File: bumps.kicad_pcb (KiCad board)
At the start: 2 copper layers, 111.1 x 65.4 mm, 126 parts, among them M1 CONN_1, M2 CONN_1, M3 CONN_1, P1 Micro-E, P10 Mot-A, P11 Mot-A, P12 Mot-X, P13 T1, P14 T2, P15 T3, P16 MPower, P17 PWM-2, P18 PWM-1, P19 END-X, P2 DIL6, P20 END-Y, P21 END-Z, P22 Mot-X, P23 Mot-Y, P24 Mot-Y, P25 Mot-Z, P26 Mot-Z, P27 Aux, P29 PWM, P3 Mot-E, P4 Mot-E, P5 DIL6, P6 DIL6, P7 DIL6, P8 P8 Header, P9 P9 Header, Q1 N-FET, Q2 N-FET, Q3 FDS9926A, Q4 FDS9926A, U1 E-Polo, U2 A-Polo, U3 X-Polo, U4 Y-Polo, U5 Z-Polo, U6 MC34063, U7 AP1117/3.3

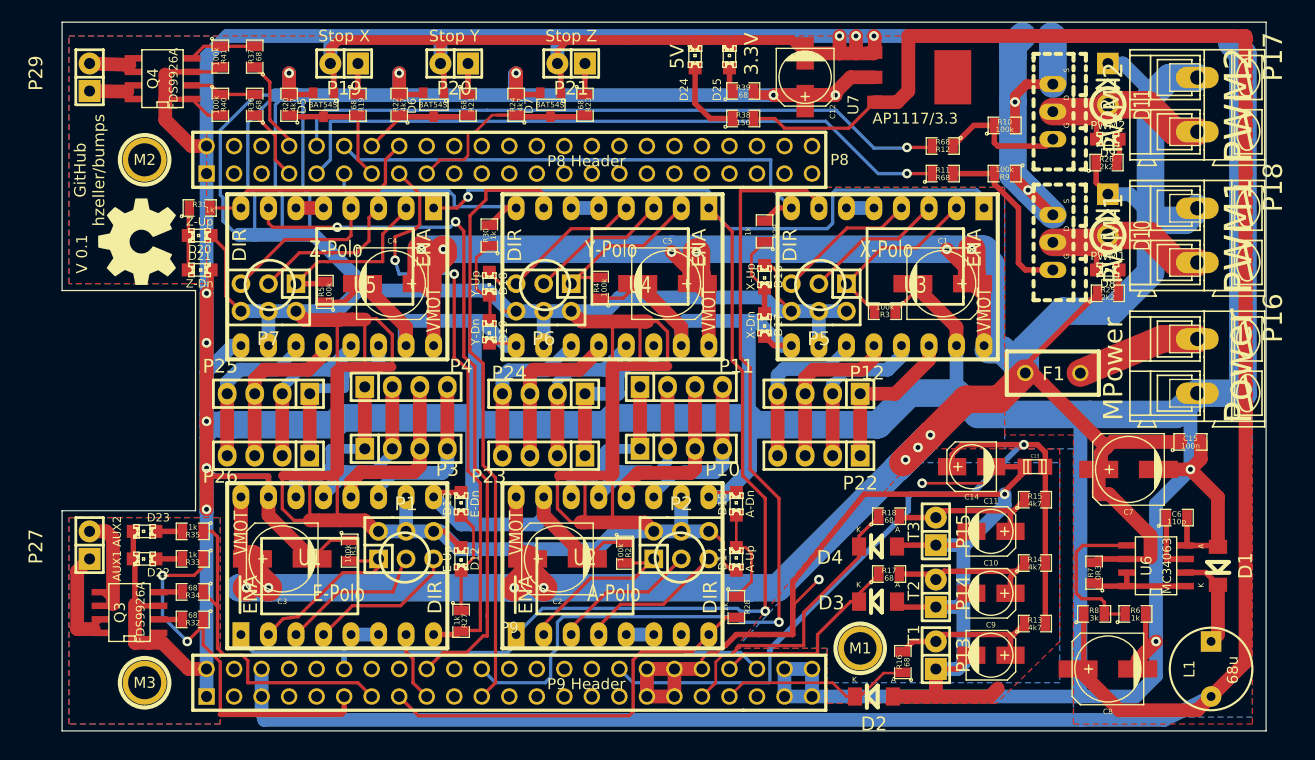
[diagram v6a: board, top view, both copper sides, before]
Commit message: o Route the new capacitors and resistors.
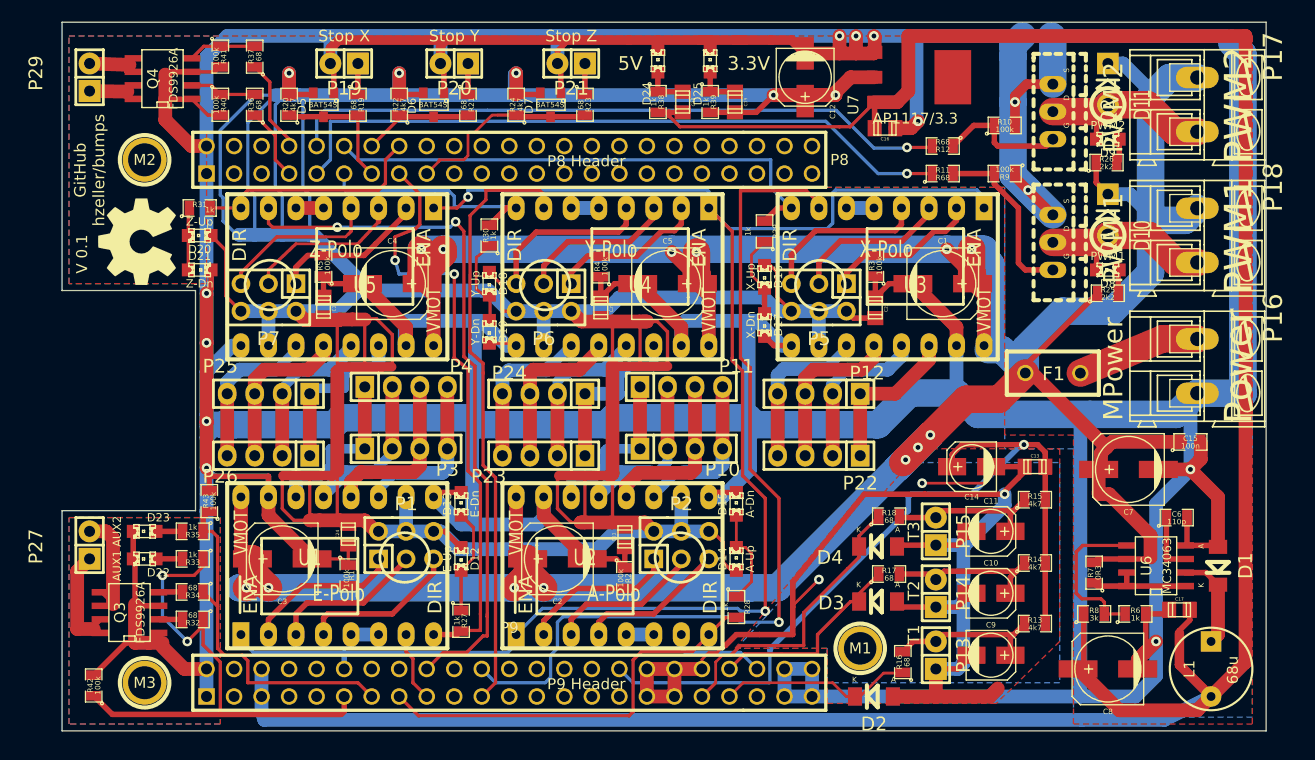
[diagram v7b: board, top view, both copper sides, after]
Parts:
- added C16: 100n, Capacitors_SMD:c_0805, F.Cu at (123.6, 37.7)
- added C17: 100n, Capacitors_SMD:c_0805, F.Cu at (150.7, 82.2)
- added C18: 100n, Capacitors_SMD:c_0805, F.Cu at (104.9, 35.3)
- added C19: 100n, Capacitors_SMD:c_0805, F.Cu at (109.7, 35.3)
- added C20: 100n, Capacitors_SMD:c_0805, F.Cu at (97.3, 54.3)
- added C21: 100n, Capacitors_SMD:c_0805, F.Cu at (99.6, 75.4)
- added C22: 100n, Capacitors_SMD:c_0805, F.Cu at (71.8, 54.2)
- added C23: 100n, Capacitors_SMD:c_0805, F.Cu at (122.7, 54.3)
- added C24: 100n, Capacitors_SMD:c_0805, F.Cu at (74.0, 75.2)
- added R42: 100k, SMD_Packages:SM0805, F.Cu at (50.5, 89.2)
- added R43: 100k, SMD_Packages:SM0805, F.Cu at (61.2, 72.1)
- R38: value 150 -> 1k
- R39: value 68 -> 1k
- moved R38 8.02 mm to (102.6, 35.3), turned to 270 degrees
- moved R3 4.28 mm to (122.7, 50.4), turned to 90 degrees
- moved D24 3.45 mm to (102.6, 31.5)
- moved R39 3.21 mm to (107.4, 35.3), turned to 270 degrees
- moved R5 2.42 mm to (71.8, 50.4)
- moved R2 2.35 mm to (99.6, 79.2)
- moved R1 2.29 mm to (74.0, 79.0)
- moved R4 1.97 mm to (97.3, 50.5)
- moved D25 1.82 mm to (107.4, 31.5)
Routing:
- net GND: track 809.0 -> 835.2 mm
- net VDD_5V: track 226.9 -> 249.3 mm
- net VDD_3V3: track 425.0 -> 444.1 mm
- net AUX_1: track 37.3 -> 49.7 mm
- net Net-(C18-Pad2): track 7.34 -> 4.09 mm
- net Net-(P7-Pad1): track 17.5 -> 14.6 mm
- net Net-(P6-Pad3): track 13.1 -> 15.7 mm
- net Net-(P5-Pad3): track 13.1 -> 15.5 mm
- net Net-(P5-Pad1): track 16.7 -> 14.3 mm
- net AUX_2: track 31.0 -> 33.1 mm
- net Net-(C19-Pad2): track 2.26 -> 4.09 mm
- net Net-(P1-Pad1): track 16.3 -> 14.6 mm
- net Net-(P5-Pad2): track 13.1 -> 14.5 mm
- net Net-(P6-Pad2): track 13.1 -> 14.5 mm
- net Net-(P6-Pad1): track 16.0 -> 14.5 mm
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
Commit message: o More copper around pads    - fuse    - mounting holes.
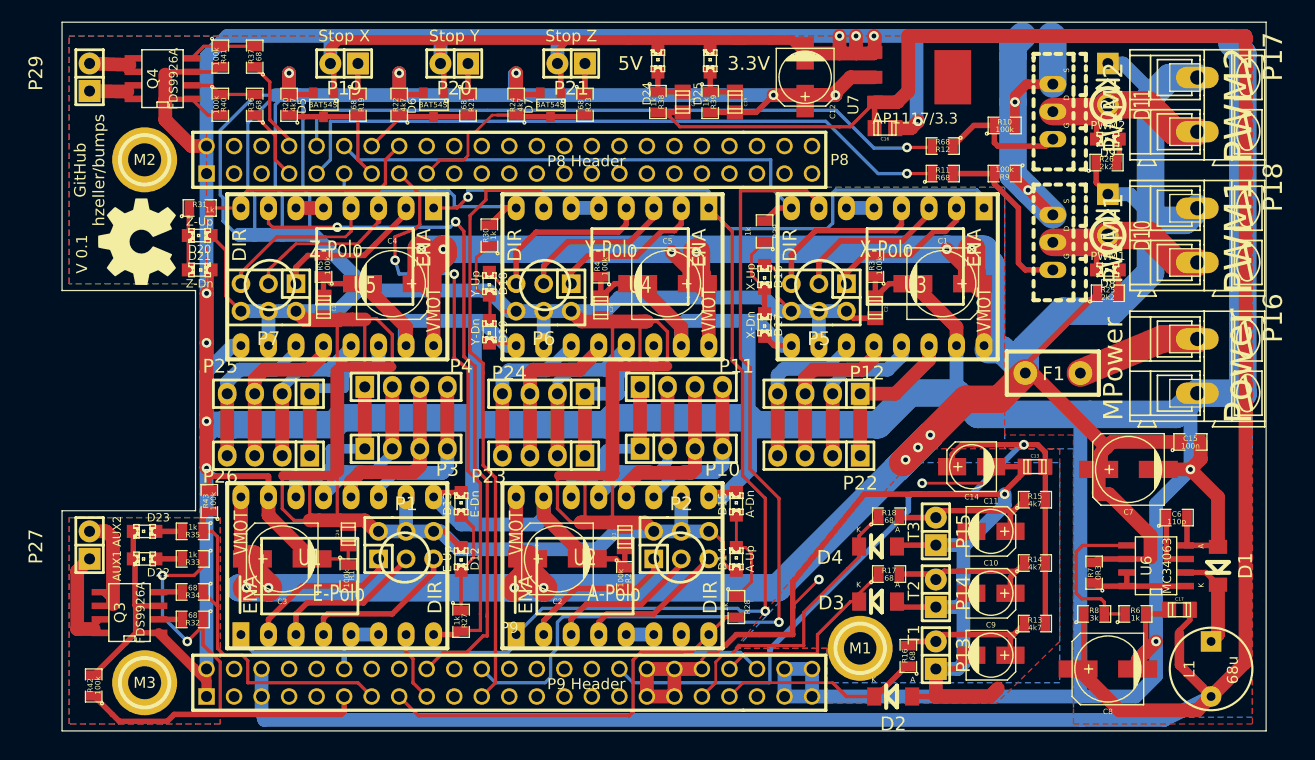
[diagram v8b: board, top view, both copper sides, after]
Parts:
- moved D2 1.78 mm to (124.3, 90.2)
- moved R16 0.76 mm to (125.7, 86.4)
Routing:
- net AGND: track 125.8 -> 124.0 mm
- net TEMP_1: track 18.0 -> 18.7 mm
- net Net-(C9-Pad1): track 14.3 -> 13.6 mm
- net AUX_1: track 49.7 -> 50.2 mm
